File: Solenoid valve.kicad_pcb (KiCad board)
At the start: 2 copper layers, 27.1 x 24.5 mm, 22 parts, among them J1 Conn_01x02, J2 Conn_01x02, J3 Conn_01x02, J4 Conn_01x02, Q1 S8050, Q2 S8050, U1 BTS443P

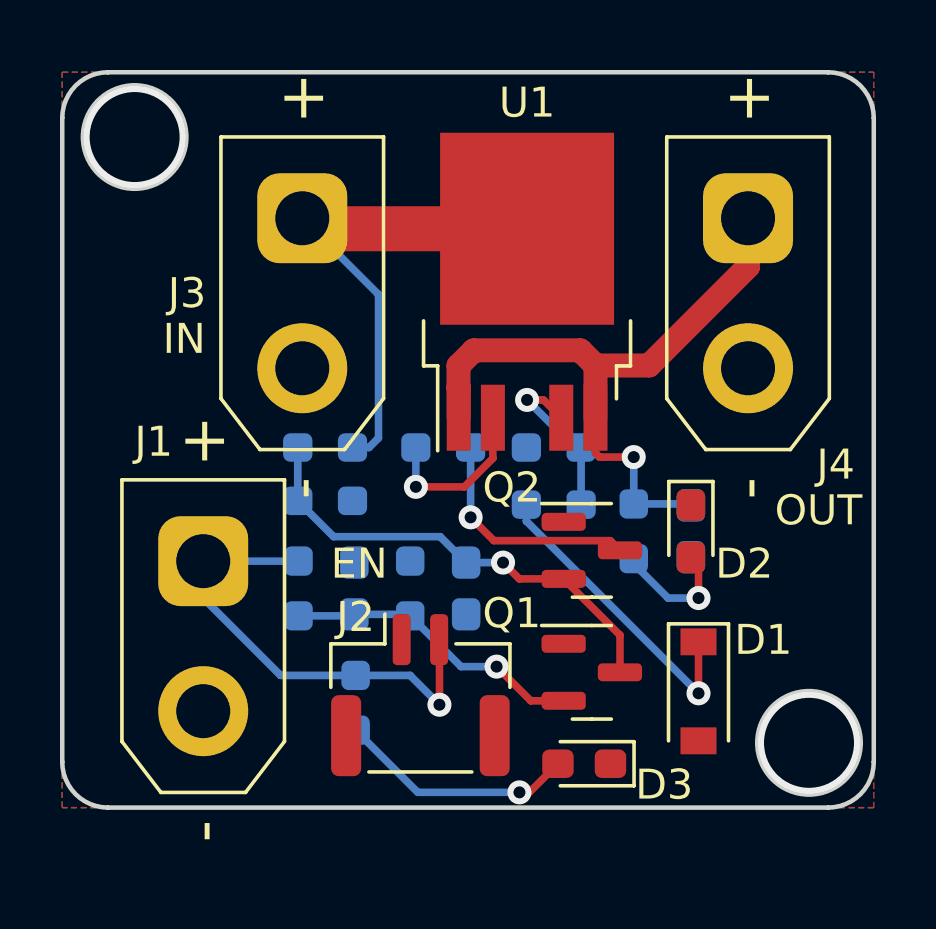
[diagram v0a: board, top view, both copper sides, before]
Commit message: Change some routings
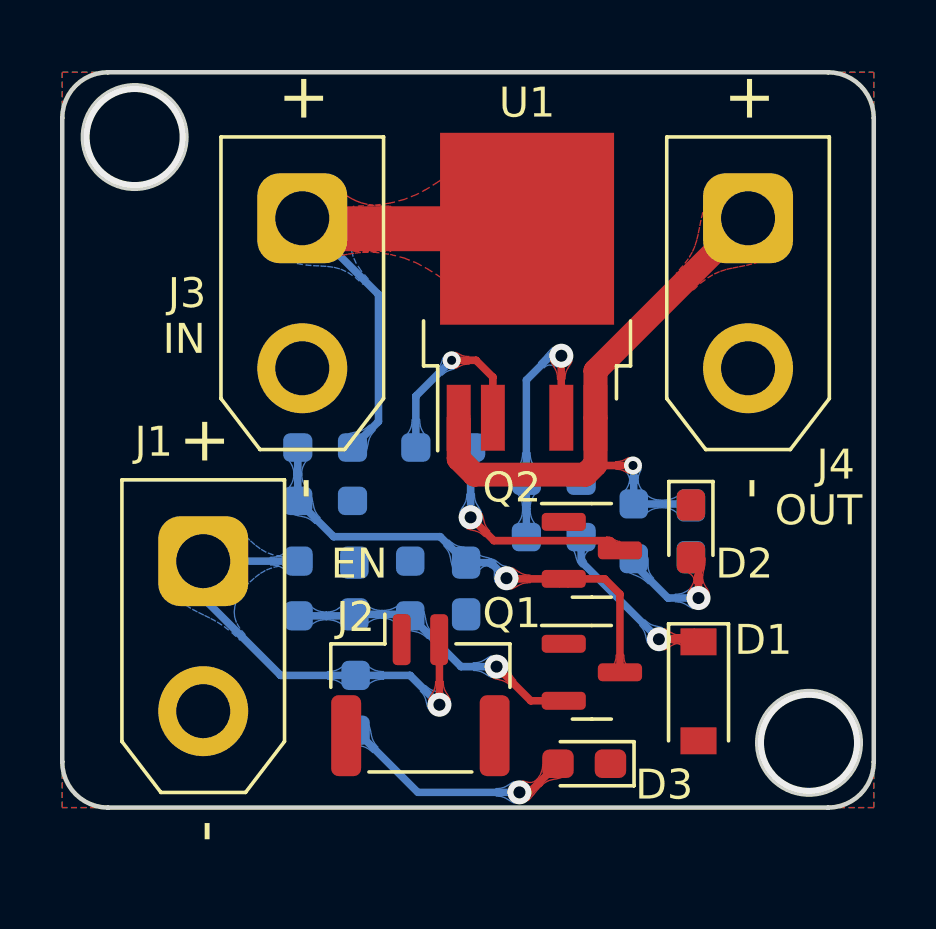
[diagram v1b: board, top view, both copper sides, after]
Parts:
- moved R6 1.11 mm to (121.5, 103.1), turned to 180 degrees
- moved R7 1.08 mm to (121.5, 105.0), turned to 0 degrees
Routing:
- net Net-(D1-Pad1): track 10.4 -> 5.83 mm
- net Net-(R6-Pad2): track 5.75 -> 8.81 mm
- net Net-(C3-Pad1): track 22.5 -> 21.1 mm
- net Net-(C2-Pad1): track 15.6 -> 16.4 mm
- net Net-(R5-Pad2): track 5.63 -> 6.36 mm

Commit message: Change some routings and S8050's footprint
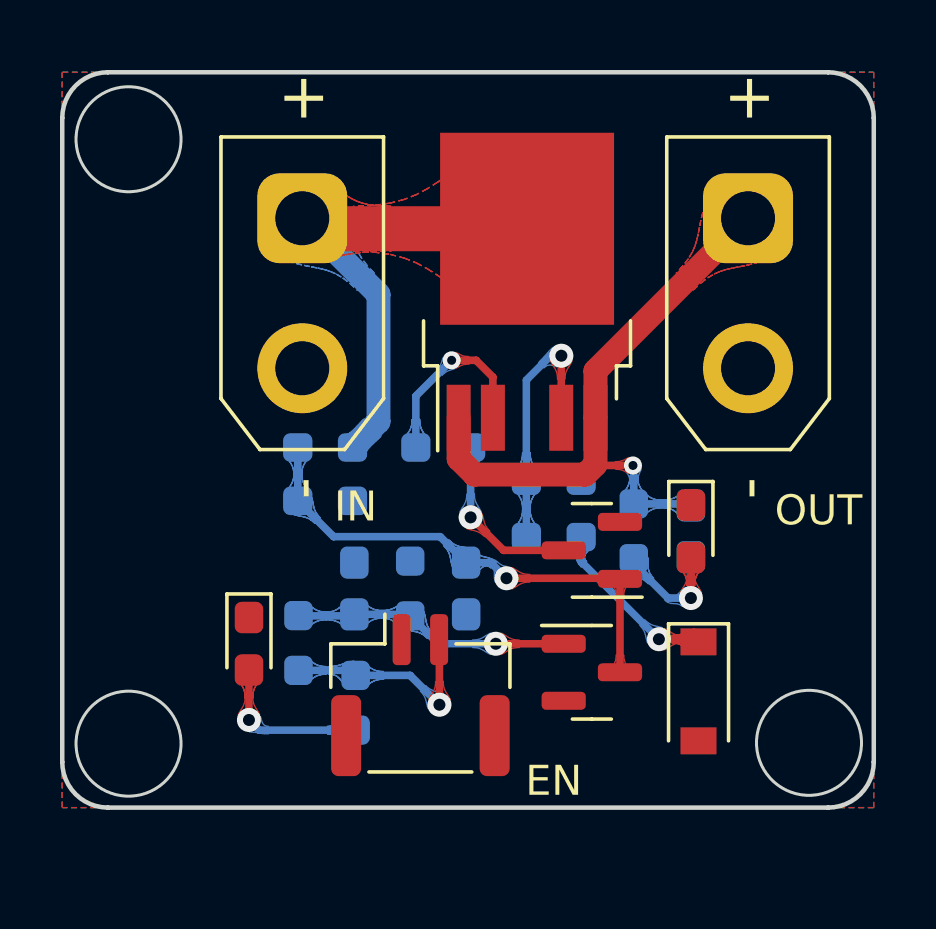
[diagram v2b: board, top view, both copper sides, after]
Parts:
- removed J1: Conn_01x02, Connector_AMASS:AMASS_XT30UPB-M_1x02_P5.0mm_Vertical
- moved D3 11.9 mm to (111.4, 108.5), turned to -90 degrees
- moved R1 1.82 mm to (113.0, 108.5), turned to 90 degrees
- turned Q2 to 180 degrees
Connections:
- J2 pad MP: Earth -> (no net)
- Q1 pad 1: Earth -> Net-(C1-Pad1)
- Q1 pad 2: Net-(C1-Pad1) -> Earth
- Q2 pad 1: Earth -> Net-(C2-Pad1)
- Q2 pad 2: Net-(C2-Pad1) -> Earth
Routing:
- net Net-(R1-Pad1): track 15.9 -> 7.35 mm
- net Net-(D3-Pad2): track 8.00 -> 5.36 mm
- net Net-(Q2-Pad3): track 7.76 -> 5.89 mm
- net Net-(C1-Pad1): track 10.1 -> 9.34 mm
- net (no net): vias 2 -> 0
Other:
- outline, holes or cut-outs redrawn

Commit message: Delete a LED
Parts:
- removed D3: LED, LED_SMD:LED_0603_1608Metric_Pad1.05x0.95mm_HandSolder
- removed R9: 2k, Resistor_SMD:R_0603_1608Metric_Pad0.98x0.95mm_HandSolder
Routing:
- net Net-(D3-Pad2): track 5.36 -> 0.00 mm, vias 1 -> 0
